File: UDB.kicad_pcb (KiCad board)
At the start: 4 copper layers, 18 x 16.5 mm, 14 parts, among them J1 TYPE-C-31-M12_13, J2 X1224WRS-04-LPV01, U1 TPD4E05U06DQAR

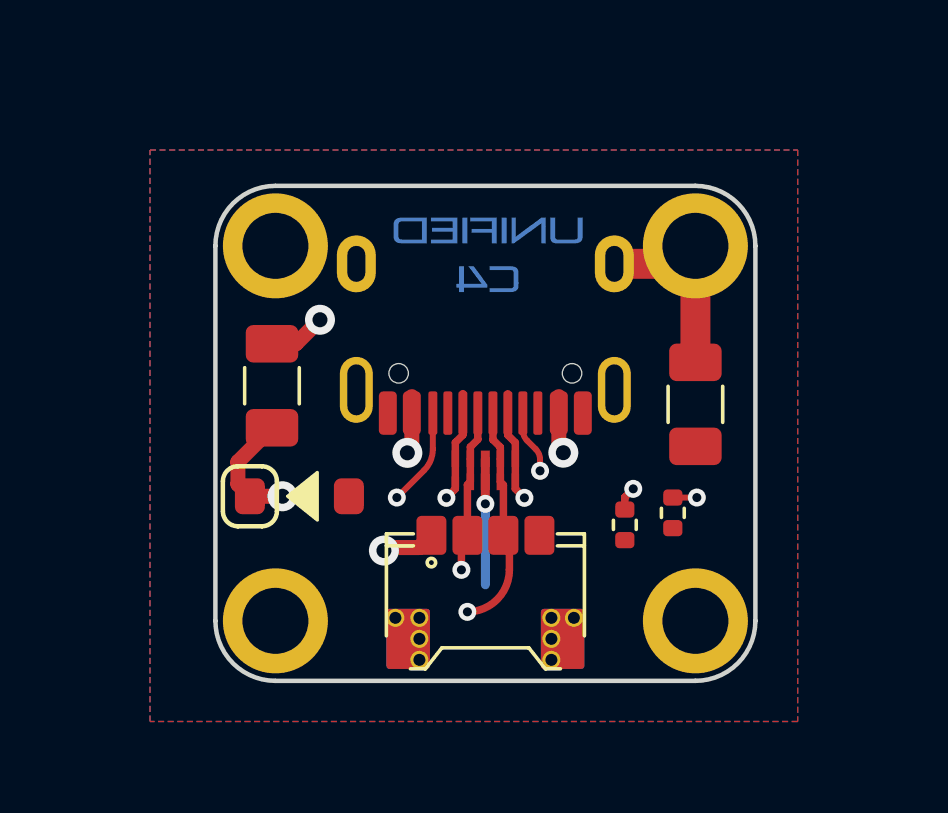
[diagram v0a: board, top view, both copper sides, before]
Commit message: New C5 version files, remove old prod files
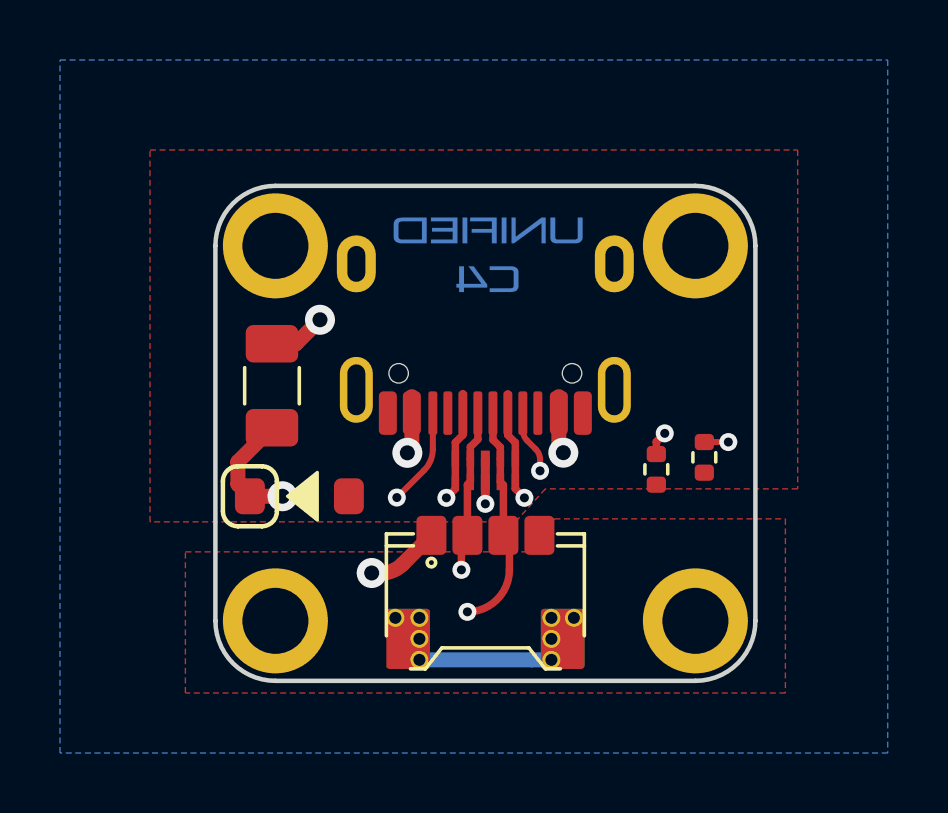
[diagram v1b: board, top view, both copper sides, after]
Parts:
- removed L1: 60R@100MHz, Inductor_SMD:L_1206_3216Metric
- moved R1 2.13 mm to (80.7, 66.0)
- moved R2 2.13 mm to (82.3, 65.6)
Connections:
- J1 pad S: GNDPWR -> GND
- MH2 pad 1: GNDPWR -> GND
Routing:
- net GNDPWR: track 6.83 -> 0.00 mm
- net GND: track 4.20 -> 6.75 mm
- net Net-(J1-CC2): track 15.6 -> 17.4 mm
- net Net-(J1-CC1): track 6.78 -> 8.55 mm
- net VCOM: track 9.83 -> 11.1 mm
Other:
- board text added: "V5.0"
- board text removed: "V4.1"
